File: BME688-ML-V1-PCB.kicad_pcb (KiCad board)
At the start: 2 copper layers, 25.4 x 25.4 mm, 29 parts, among them SW1 434133025816, U1 STM32L431KBU6TR, U2 BME688

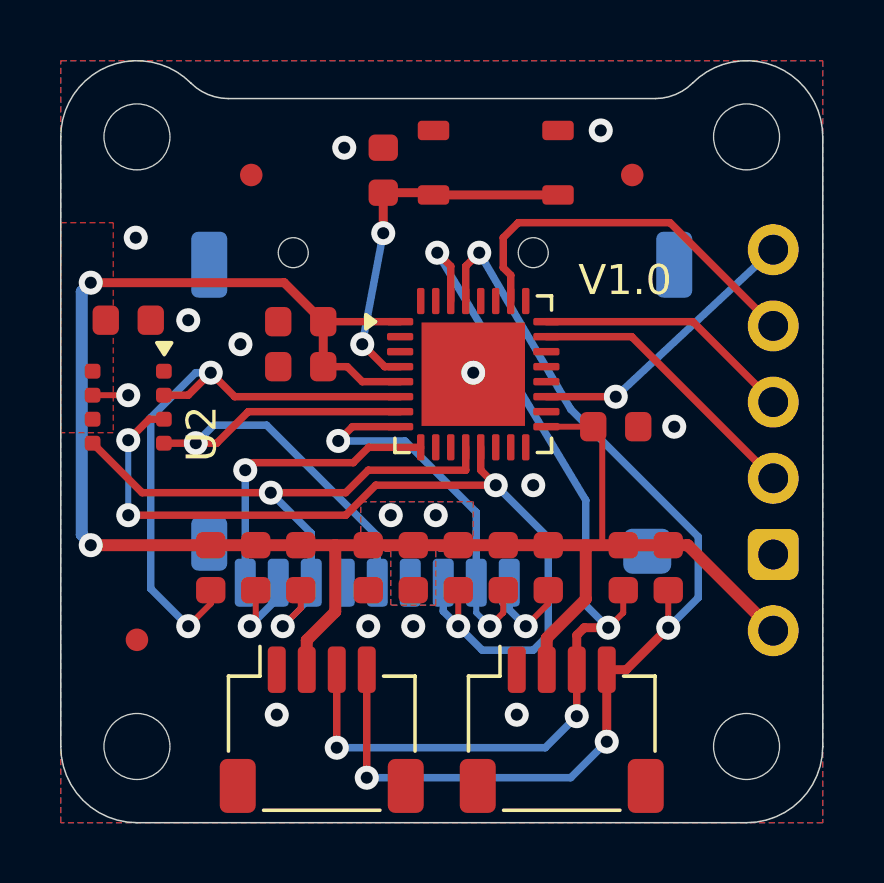
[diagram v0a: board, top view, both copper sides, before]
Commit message: fix
Tie BOOT0/PH3 to GND, as without the SW is not running stable..
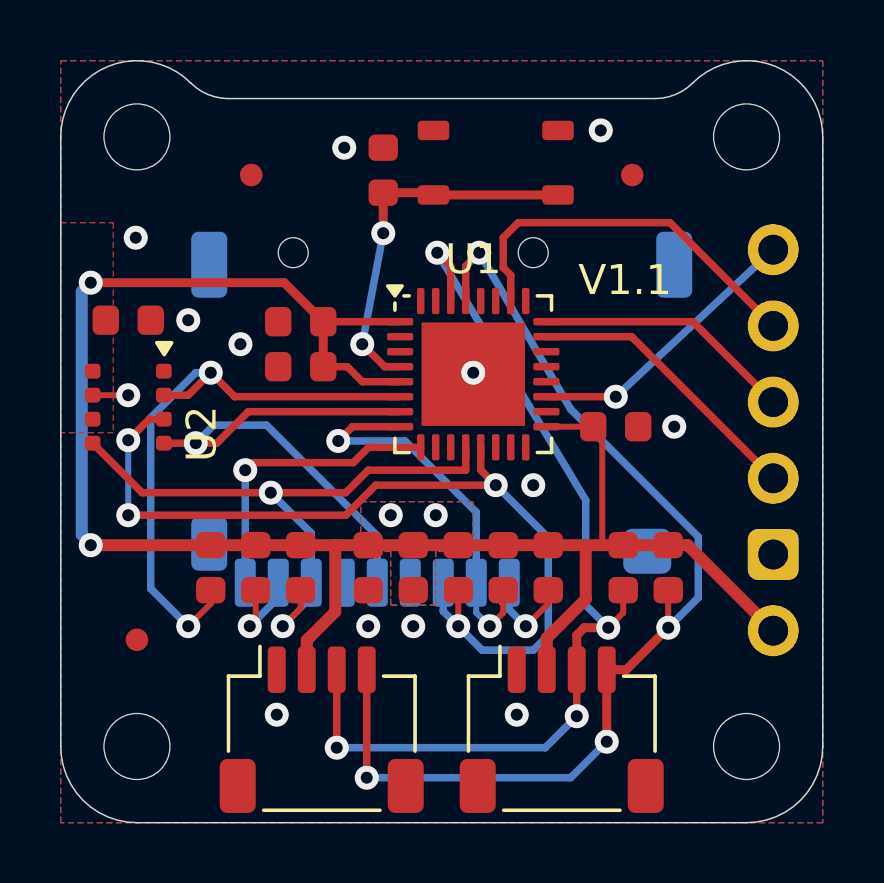
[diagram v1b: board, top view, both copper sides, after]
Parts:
- U1: footprint 1projectLibrary:STM32-QFN-32-1EP -> Package_DFN_QFN:QFN-32-1EP_5x5mm_P0.5mm_EP3.45x3.45mm
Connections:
- U1 pad 31: unconnected-(U1-PH3-Pad31) -> GND
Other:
- board text added: "V1.1"
- board text removed: "V1.0"

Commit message: Redesign for V1.2
Moved BME688 onto its own I2C bus.
Placed 2 BME688
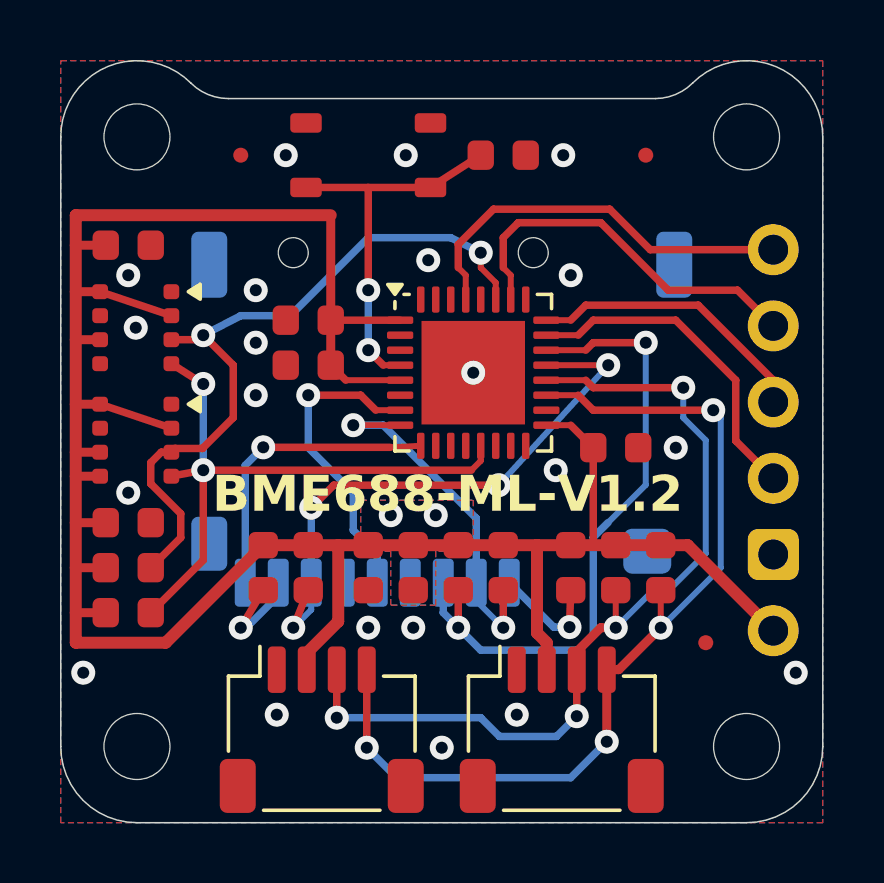
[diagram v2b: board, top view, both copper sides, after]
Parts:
- added C8: KGM15AR71C104KT, 1projectLibrary:C_0603_nominal, F.Cu at (116.5, 78.9)
- added R9: CR0603-FX-4701ELF, 1projectLibrary:R_0603_nominal, F.Cu at (116.5, 80.4)
- added U3: BME688, 1projectLibrary:BME688, F.Cu at (116.8, 76.2)
- CONN3: footprint 1GlobalFootprintsLibrary:MSD-1-A -> 1projectLibrary:MSD-1-A
- F1, F2, F3: footprint Fiducial:Fiducial_0.75mm_Mask1.5mm -> Fiducial:Fiducial_0.5mm_Mask1mm
- moved F1 19.0 mm to (135.8, 82.9)
- moved R7 12.0 mm to (132.8, 80.4)
- moved R2 10.5 mm to (122.5, 80.4)
- moved R4 9.00 mm to (131.3, 80.4)
- moved R5 8.00 mm to (121.0, 80.4)
- moved R3 5.50 mm to (129.1, 80.4)
- moved SW1 4.26 mm to (124.5, 66.7)
- moved C6 4.03 mm to (129.1, 66.7), turned to 0 degrees
- moved R6 3.75 mm to (134.3, 80.4)
- moved R8 3.13 mm to (116.5, 81.9), turned to 0 degrees
- moved U2 2.66 mm to (116.8, 72.4)
- moved C3 2.50 mm to (116.5, 69.7)
- moved F3 0.80 mm to (133.8, 66.7)
- moved F2 0.75 mm to (120.3, 66.7)
- moved C7 0.70 mm to (132.8, 76.4)
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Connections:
- CONN1 pad 3: I2C-SDA -> I2C1-SDA
- CONN1 pad 4: I2C-SCL -> I2C1-SCL
- CONN2 pad 3: I2C-SDA -> I2C1-SDA
- CONN2 pad 4: I2C-SCL -> I2C1-SCL
- R2 pad 2: I2C-SDA -> SPI-MISO
- R3 pad 2: I2C-SCL -> CS-SDCARD
- R4 pad 2: SPI-MISO -> Net-(CONN3-NC1)
- R5 pad 2: CS-SDCARD -> Net-(CONN3-NC8)
- R6 pad 2: Net-(CONN3-NC1) -> I2C1-SCL
- R7 pad 2: Net-(CONN3-NC8) -> I2C1-SDA
- R8 pad 2: CS-BME68X -> I2C3-SCL
- U1 pad 10: unconnected-(U1-PA4-Pad10) -> GND
- U1 pad 11: unconnected-(U1-PA5-Pad11) -> GND
- U1 pad 12: SPI-MISO -> GND
- U1 pad 13: SPI-MOSI -> I2C3-SCL
- U1 pad 14: unconnected-(U1-PB0-Pad14) -> GND
- U1 pad 15: unconnected-(U1-PB1-Pad15) -> GND
- U1 pad 18: unconnected-(U1-PA8-Pad18) -> GND
- U1 pad 19: UART1-TX -> I2C1-SCL
- U1 pad 2: unconnected-(U1-PC14-Pad2) -> GND
- U1 pad 20: unconnected-(U1-USART1-RX-Pad20) -> I2C1-SDA
- U1 pad 21: unconnected-(U1-PA11-Pad21) -> SPI-MISO
- U1 pad 22: unconnected-(U1-PA12-Pad22) -> SPI-MOSI
- U1 pad 25: unconnected-(U1-PA15-Pad25) -> GND
- U1 pad 27: unconnected-(U1-PB4-Pad27) -> I2C3-SDA
- U1 pad 28: unconnected-(U1-PB5-Pad28) -> GND
- U1 pad 29: I2C-SCL -> UART1-TX
- U1 pad 3: unconnected-(U1-PC15-Pad3) -> GND
- U1 pad 30: I2C-SDA -> GND
- U1 pad 6: CS-BME68X -> GND
- U2 pad 2: CS-BME68X -> +3.3V
- U2 pad 3: SPI-MOSI -> I2C3-SDA
- U2 pad 4: SPI1-CLK -> I2C3-SCL
- U2 pad 5: SPI-MISO -> GND
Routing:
- net I2C-SCL: track 35.7 -> 0.00 mm, vias 4 -> 0
- net I2C-SDA: track 32.3 -> 0.00 mm, vias 4 -> 0
- net I2C1-SCL: track 0.00 -> 31.5 mm, vias 0 -> 4
- net I2C1-SDA: track 0.00 -> 29.7 mm, vias 0 -> 4
- net I2C3-SDA: track 0.00 -> 24.4 mm, vias 0 -> 2
- net +3.3V: track 62.9 -> 85.4 mm, vias 4 -> 2
- net I2C3-SCL: track 0.00 -> 20.6 mm, vias 0 -> 2
- net CS-BME68X: track 20.1 -> 0.00 mm, vias 2 -> 0
- net SPI-MOSI: track 30.2 -> 21.9 mm, vias 4 -> 2
- net SPI1-CLK: track 17.7 -> 10.5 mm
- net UART1-TX: track 9.49 -> 13.5 mm, vias 1 -> 0
- net SWDIO: track 9.52 -> 11.1 mm
- net SPI-MISO: track 21.0 -> 19.6 mm, vias 2 -> 4
- net GND: track 1.19 -> 0.00 mm, vias 13 -> 21
- net CS-SDCARD: track 13.2 -> 12.2 mm
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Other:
- board text added: "BME688-ML-V1.2"
- board text removed: "V1.1"

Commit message: Add CC logo
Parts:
- added G***: LOGO, 1projectLibrary:CC-logo-14mm, B.Cu at (127.1, 85.5)
